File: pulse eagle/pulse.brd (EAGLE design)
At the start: 21.3 x 31.7 mm, 24 parts, among them IC1 LM358D, J1 ISP Touch, T1 BC846, Y1 8MHz

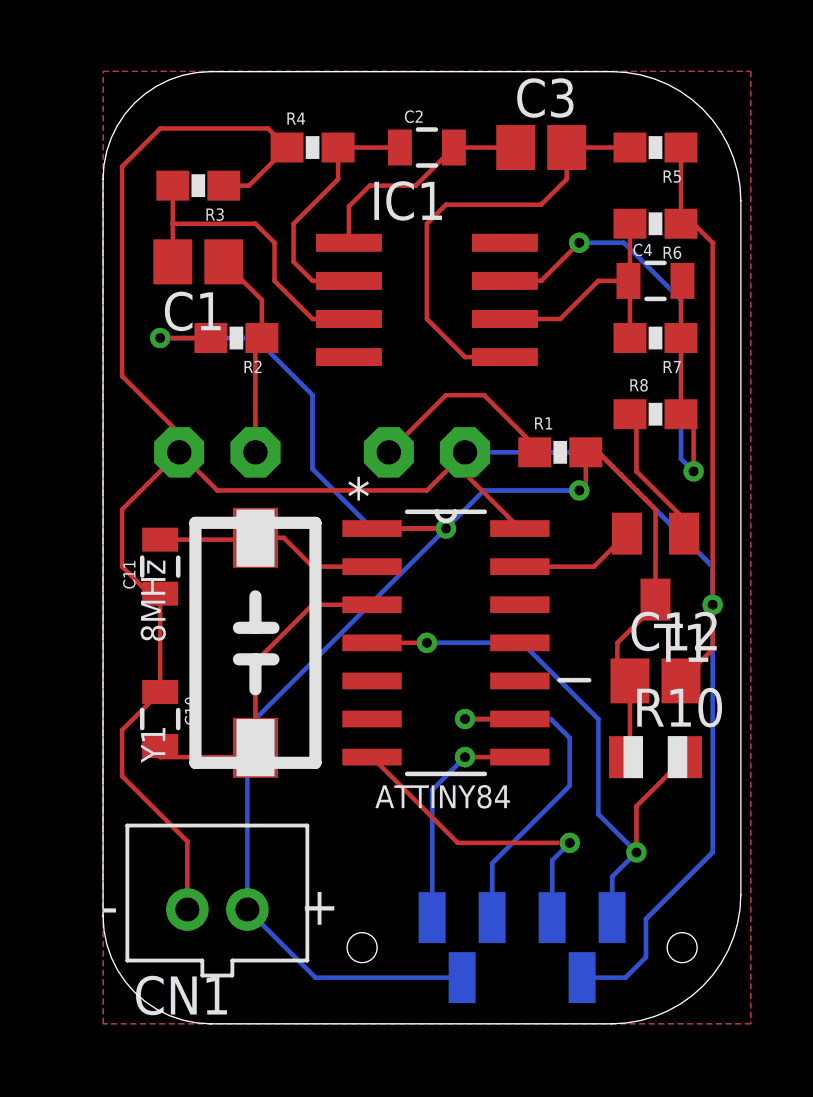
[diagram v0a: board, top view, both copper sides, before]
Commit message: Invoking power/ground on op amp, fixing dimension, drawing polarized lines for tantalum caps, and adjusting labels.
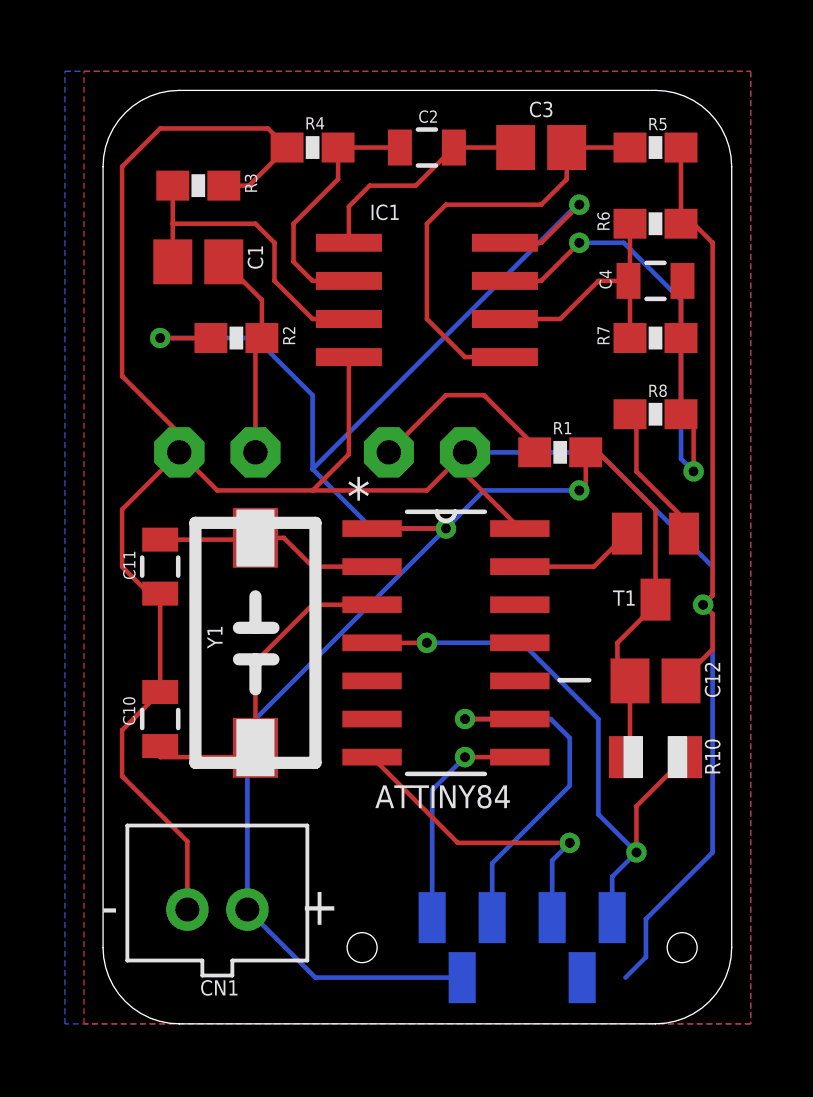
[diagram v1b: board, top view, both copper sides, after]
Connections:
- removed net V+: IC1.8
- removed net V-: IC1.4
- net GND: now also IC1.4
- net VCC: now also IC1.8
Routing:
- net VCC: track 59.8 -> 75.3 mm, vias 3 -> 4
- net GND: track 96.4 -> 100.4 mm
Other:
- board size 21.3 x 31.7 mm -> 21 x 31.1 mm
